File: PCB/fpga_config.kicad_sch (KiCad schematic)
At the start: 18 parts, among them J2 Molex 0878321420, U2 XC7A50T-FGG484

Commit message: Version 1.2 routed
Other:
- title: FPGA Bank 0 (Config) -> Pi 5 - Artix XC7A50T - PCIe FPGA Hat
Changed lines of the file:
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@@
 	(paper "A4")
 	(title_block
-		(title "FPGA Bank 0 (Config)")
-		(date "2024-03-24")
-		(rev "1.1")
+		(title "Pi 5 - Artix XC7A50T - PCIe FPGA Hat")
+		(date "2025-07-17")
+		(rev "1.2")
 		(company "George Smart, M1GEO")
 		(comment 1 "https://github.com/m1geo/Pi5-Artix-FPGA-Hat")

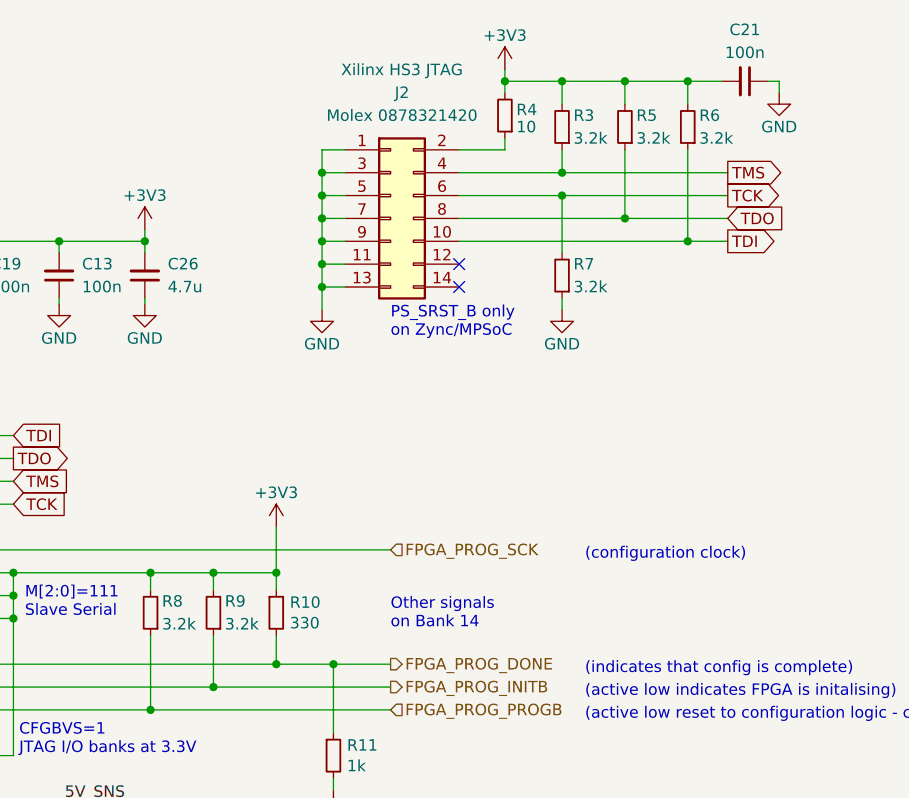
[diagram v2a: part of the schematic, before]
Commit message: Updating LEDs footprint and Resistors value
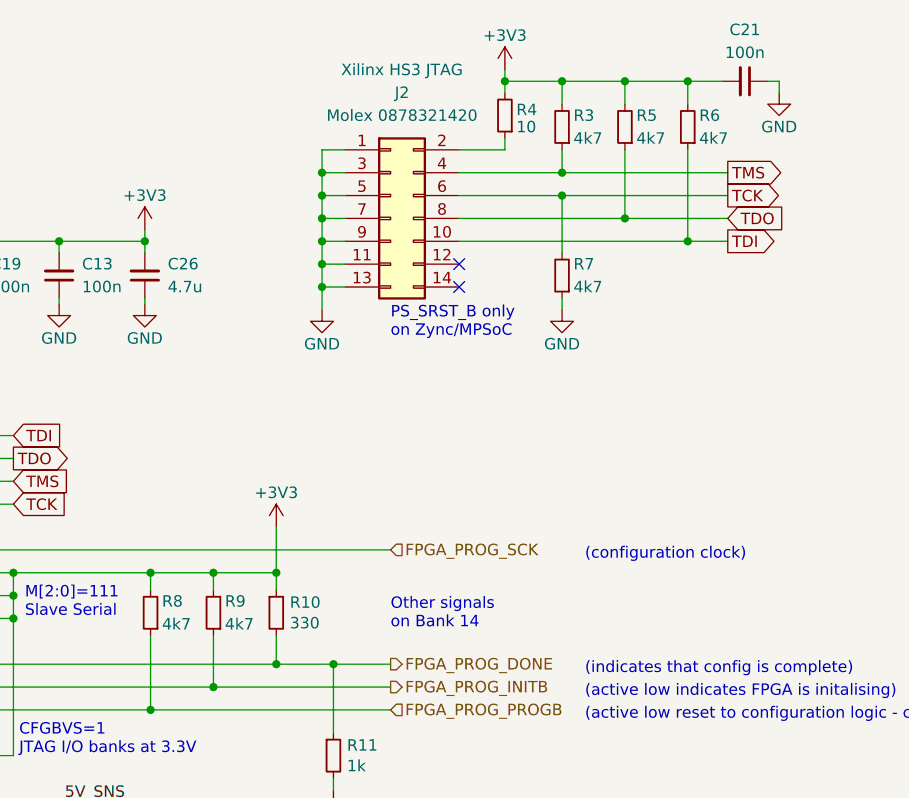
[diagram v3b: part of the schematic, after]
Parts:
- D1: footprint LED_SMD:LED_0402_1005Metric -> LED_SMD:LED_0603_1608Metric
- R3, R5, R6, R7, R8, R9: value 3.2k -> 4k7; LCSC C853935 -> C25900
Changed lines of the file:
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@@
 			)
 		)
-		(property "Value" "3.2k"
+		(property "Value" "4k7"
 			(at 168.275 36.83 0)
 			(effects
@@
 			)
 		)
-		(property "LCSC" "C853935"
+		(property "LCSC" "C25900"
 			(at 167.005 35.56 0)
 			(effects
@@
 			)
 		)
-		(property "Value" "3.2k"
+		(property "Value" "4k7"
 			(at 122.555 90.805 0)
 			(effects
@@
 			)
 		)
-		(property "LCSC" "C853935"
+		(property "LCSC" "C25900"
 			(at 121.285 89.535 0)
 			(effects
@@
 			)
 		)
-		(property "Footprint" "LED_SMD:LED_0402_1005Metric"
+		(property "Footprint" "LED_SMD:LED_0603_1608Metric"
 			(at 134.62 113.03 0)
 			(effects
@@
 			)
 		)
-		(property "Value" "3.2k"
+		(property "Value" "4k7"
 			(at 115.57 90.805 0)
 			(effects
@@
 			)
 		)
-		(property "LCSC" "C853935"
+		(property "LCSC" "C25900"
 			(at 114.3 89.535 0)
 			(effects
@@
 			)
 		)
-		(property "Value" "3.2k"
+		(property "Value" "4k7"
 			(at 161.29 53.34 0)
 			(effects
@@
 			)
 		)
-		(property "LCSC" "C853935"
+		(property "LCSC" "C25900"
 			(at 160.02 52.07 0)
 			(effects
@@
 			)
 		)
-		(property "Value" "3.2k"
+		(property "Value" "4k7"
 			(at 161.29 36.83 0)
 			(effects
@@
 			)
 		)
-		(property "LCSC" "C853935"
+		(property "LCSC" "C25900"
 			(at 160.02 35.56 0)
 			(effects
@@
 			)
 		)
-		(property "Value" "3.2k"
+		(property "Value" "4k7"
 			(at 175.26 36.83 0)
 			(effects
@@
 			)
 		)
-		(property "LCSC" "C853935"
+		(property "LCSC" "C25900"
 			(at 173.99 35.56 0)
 			(effects
